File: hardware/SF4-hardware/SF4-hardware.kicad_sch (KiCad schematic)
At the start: 2 parts, among them U1 CD4053B

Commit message: Modified simulation and harware files
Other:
- moved on the sheet: A1

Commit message: Added kicad backup files
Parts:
- added PS1: IA0505S, Converter_DCDC:Converter_DCDC_XP_POWER-IAxxxxS_THT, symbol Converter_DCDC:IA0505S
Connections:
- net +5V: now also PS1.1 (+Vin)
- net GND: now also PS1.2 (-Vin), PS1.5 (0V)
- new net +5VA: PS1.6 (+Vout)
- new net -5VA: PS1.4 (-Vout)

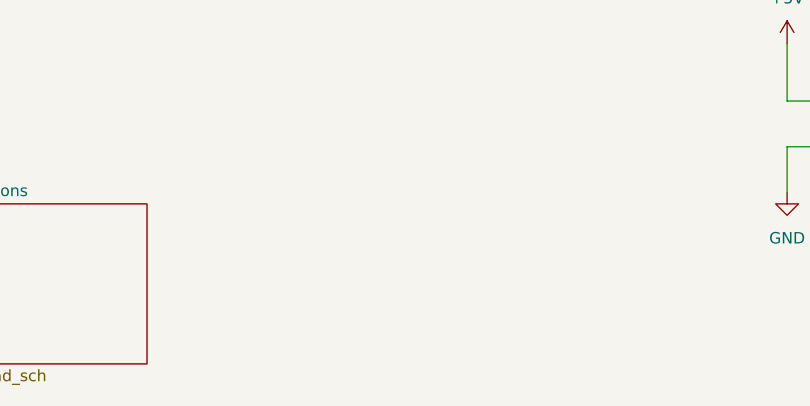
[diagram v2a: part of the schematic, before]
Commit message: Added new ECG circuit
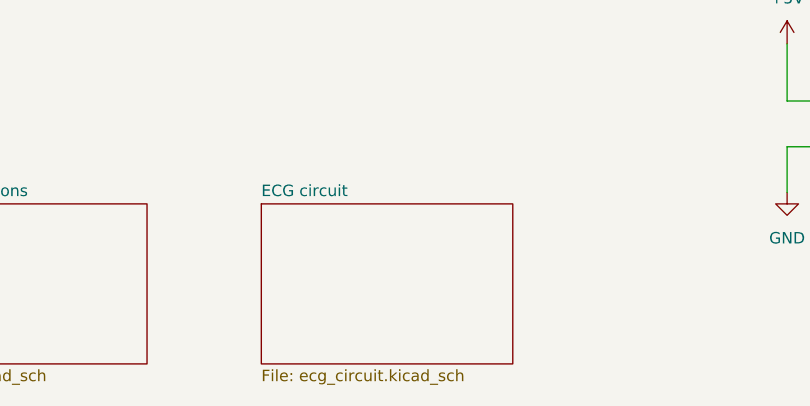
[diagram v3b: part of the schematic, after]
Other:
- added sheet ECG circuit (ecg_circuit.kicad_sch)
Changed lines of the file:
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@@
+		)
+	)
+	(sheet
+		(at 120.65 139.7)
+		(size 27.94 17.78)
+		(fields_autoplaced yes)
+		(stroke
+			(width 0.1524)
+			(type solid)
+		)
+		(fill
+			(color 0 0 0 0.0000)
+		)
+		(property "Sheetname" "ECG circuit"
+			(at 120.65 138.9884 0)
+			(effects
+				(font
+					(size 1.27 1.27)
+				)
+				(justify left bottom)
+			)
+		)
+		(property "Sheetfile" "ecg_circuit.kicad_sch"
+			(at 120.65 158.0646 0)
+			(effects
+				(font
+					(size 1.27 1.27)
+				)
+				(justify left top)
+			)
+		)
+		(instances
+			(project "SF4-hardware"
+				(path "/ef5111bd-e8db-4b6d-9a36-6e7b6428b384"
+					(page "4")
+				)
+			)
 		)
 	)

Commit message: Added changes to hardware
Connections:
- net Electrode C2 is gone; now on net Right Arm Electrode: U1.3 (C1)
- net D2: now also U1.10 (S2); no longer U1.11 (S1)
- net D3: now also U1.9 (S3); no longer U1.10 (S2)
- net D4: now also U1.6 (INH); no longer U1.9 (S3)
- net A1: no longer names the net of A1.10 (A1)
- net A2: no longer names the net of A1.11 (A2)
- net D5: no longer names the net of A1.20 (D5)
- net D5: no longer U1.6 (INH)
- net Electrode A: no longer names the net of U1.14 (A)
- net Electrode A1: no longer names the net of U1.12 (A0)
- net Electrode A2: no longer names the net of U1.13 (A1)
- net Electrode B renamed Electrode 1
- net Electrode B1 renamed Right Arm Electrode
- net Electrode B2 renamed Left Arm Electrode
- net Electrode C renamed Electrode 2
- net Electrode C1 renamed Left Leg Electrode
- no-connect marks 21 -> 28
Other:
- removed sheet Amplifiers
- removed sheet Multiplexer Connections
- note added: "Dual Power Supply"
- note added: "Green"
- note added: "Inhibit low for signal flow!"
- note added: "LALL: B: High C: Low"
- note added: "LARA: B: High C: High"
- note added: "Orange"
- note added: "RALL: B: Low C: Low"
- note added: "Yellow"
- moved on the sheet: PS1
